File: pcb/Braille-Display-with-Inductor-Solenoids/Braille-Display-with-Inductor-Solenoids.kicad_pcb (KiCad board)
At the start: 2 copper layers, 90 x 89 mm, 203 parts, among them J1 Screw_Terminal_01x02, J2 Screw_Terminal_01x02, J3 Screw_Terminal_01x02, J4 Conn_01x03, J5 Conn_01x02, J6 Conn_01x08, SW1 SW_Push, SW2 SW_Push, U1 RP2040-Zero, U10 AD116, U11 AD116, U12 AD116, U13 AD116, U14 AD116, U15 AD116, U16 AD116, U17 AD116, U18 AD116, U19 AD116, U2 AD116, U20 AD116, U21 AD116, U22 AD116, U23 AD116, U24 AD116, U25 AD116, U26 74HC595, U27 74HC595, U28 74HC595, U29 74HC595, U3 AD116, U30 74HC595, U31 74HC595, U4 AD116, U5 AD116, U6 AD116, U7 AD116, U8 AD116, U9 AD116

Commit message: Clean up reference designator silkscreens, add layers
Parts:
- C1: moved to F.Cu
- moved U28 51.8 mm to (37.0, 76.0), turned to 180 degrees
- moved U27 50.3 mm to (37.0, 89.5), turned to 180 degrees
- moved U26 49.0 mm to (37.0, 103.5), turned to 180 degrees
- moved U29 17.4 mm to (83.0, 103.5), turned to 0 degrees
- moved U30 12.0 mm to (83.0, 89.5), turned to 0 degrees
- moved U31 7.18 mm to (83.0, 76.0), turned to 0 degrees
- moved D1 2.48 mm to (95.6, 114.5)
- moved R1 2.48 mm to (95.6, 118.4)
- moved J3 1.50 mm to (102.0, 115.5)
- moved C1 1.22 mm to (107.8, 105.2)
- moved H4 1.00 mm to (115.0, 115.0)
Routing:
- net /UART0_TX: track 0.00 -> 6.19 mm
- net /UART0_RX: track 0.00 -> 6.00 mm
- net +3V3: track 0.00 -> 1.76 mm, vias 0 -> 7
- net VDC: vias 0 -> 24
- net GND: vias 0 -> 30
- added copper zone on B.Cu, net +3V3
- added copper zone on In2.Cu, net GND
- added copper zone on In1.Cu, net VDC
- removed copper zone on B.Cu, net GND
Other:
- board size 90 x 89 mm -> 90 x 90 mm
- copper layers 2 -> 4
- board text added: "2.5mm Intra-Cell Pitch. 6mm Inter-Cell Pitch X. For 0805 (2012 Metric) vertical SMD, chip is 2mm long. Use 1.6mm PCB. Top (Red) = GND In1 (Green) = VDC In2 (Orange) = GND Bottom (Blue) = 3V3"
- board text removed: "2.5mm Intra-Cell Pitch. 6mm Inter-Cell Pitch X. For 0805 (2012 Metric) vertical SMD, chip is 2mm long. Use 1.6mm PCB."

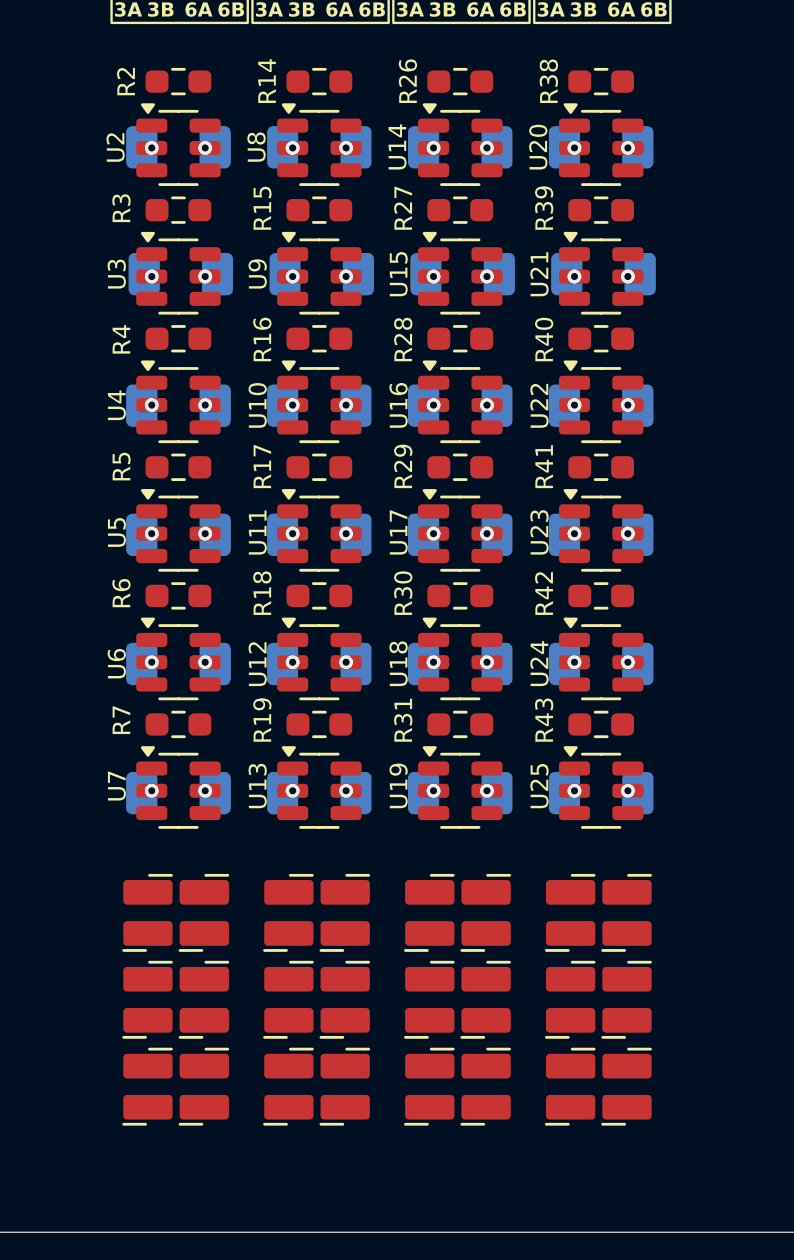
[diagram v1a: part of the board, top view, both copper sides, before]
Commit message: Fix braille LED swap
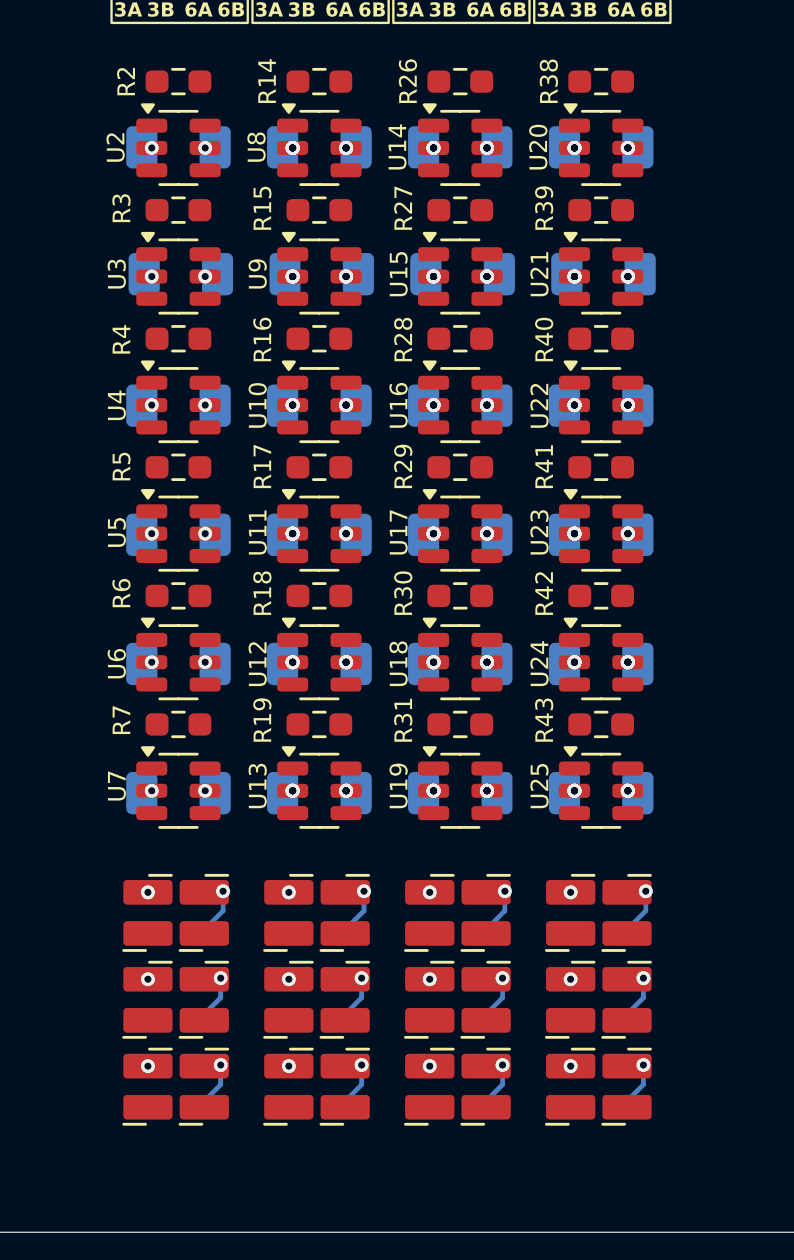
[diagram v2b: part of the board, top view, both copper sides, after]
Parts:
- moved D11 7.40 mm to (58.3, 106.4)
- moved D17 7.40 mm to (64.3, 106.4)
- moved D23 7.40 mm to (70.3, 106.4)
- moved D5 7.40 mm to (52.3, 106.4)
- moved D13 3.70 mm to (58.3, 113.8)
- moved D19 3.70 mm to (64.3, 113.8)
- moved D25 3.70 mm to (70.3, 113.8)
- moved D7 3.70 mm to (52.3, 113.8)
- moved D12 3.70 mm to (58.3, 110.1)
- moved D18 3.70 mm to (64.3, 110.1)
- moved D24 3.70 mm to (70.3, 110.1)
- moved D6 3.70 mm to (52.3, 110.1)
- turned R13 to 0 degrees
- turned R25 to 0 degrees
- turned R37 to 0 degrees
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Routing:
- net Net-(D7-AK): track 0.00 -> 2.23 mm, vias 0 -> 1
- net Net-(D6-AK): track 0.00 -> 2.23 mm, vias 0 -> 1
- net Net-(D25-AK): track 0.00 -> 2.23 mm, vias 0 -> 1
- net Net-(D24-AK): track 0.00 -> 2.23 mm, vias 0 -> 1
- net Net-(D19-AK): track 0.00 -> 2.23 mm, vias 0 -> 1
- net Net-(D18-AK): track 0.00 -> 2.23 mm, vias 0 -> 1
- net Net-(D13-AK): track 0.00 -> 2.23 mm, vias 0 -> 1
- net Net-(D12-AK): track 0.00 -> 2.23 mm, vias 0 -> 1
- net Net-(D5-AK): track 0.00 -> 2.23 mm, vias 0 -> 1
- net Net-(D11-AK): track 0.00 -> 2.23 mm, vias 0 -> 1
- net Net-(D23-AK): track 0.00 -> 2.23 mm, vias 0 -> 1
- net Net-(D17-AK): track 0.00 -> 2.23 mm, vias 0 -> 1
- net VDC: vias 24 -> 60
- net Net-(D9-AK): vias 0 -> 1
- net Net-(D8-AK): vias 0 -> 1
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
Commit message: Finish routing and review
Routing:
- net GND: track 0.00 -> 361.1 mm, vias 66 -> 41
- net VDC: track 0.00 -> 201.3 mm, vias 60 -> 29
- net +3V3: track 1.76 -> 182.3 mm, vias 7 -> 10
- net /~{SHIFT_SRCLR}: track 0.00 -> 148.0 mm, vias 0 -> 6
- net /SHIFT_RCLK: track 0.00 -> 142.7 mm, vias 0 -> 5
- net /SHIFT_SRCK: track 0.00 -> 141.2 mm, vias 0 -> 6
- net /~{SHIFT_OE}: track 0.00 -> 136.5 mm, vias 0 -> 2
- net /SHIFT_SER_IN: track 0.00 -> 92.4 mm, vias 0 -> 1
- net Net-(U28-QH'): track 0.00 -> 83.9 mm, vias 0 -> 3
- net Net-(B3-6B): track 0.00 -> 71.3 mm, vias 0 -> 2
- net /Braille_Cells_and_Controls/Braille_Cell3/DOT6_A: track 0.00 -> 70.9 mm, vias 0 -> 3
- net Net-(B4-6B): track 0.00 -> 70.8 mm, vias 0 -> 2
- net /Braille_Cells_and_Controls/Braille_Cell1/DOT6_A: track 0.00 -> 70.7 mm, vias 0 -> 3
- net /Braille_Cells_and_Controls/Braille_Cell3/DOT5_A: track 0.00 -> 70.6 mm, vias 0 -> 4
- net Net-(B4-4B): track 0.00 -> 70.2 mm, vias 0 -> 2
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- added copper zone on F.Cu, net +5V

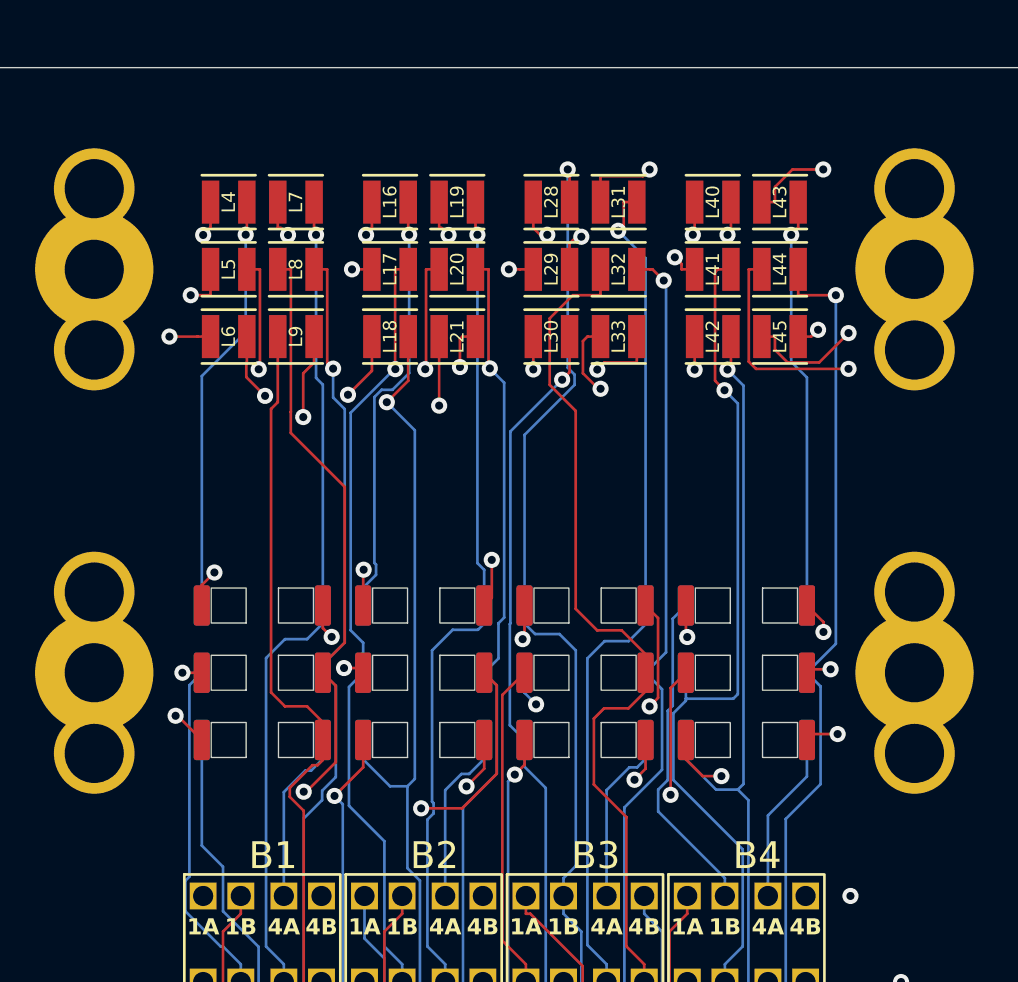
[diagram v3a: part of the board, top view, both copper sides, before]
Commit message: Update SMD solenoid with THT pads
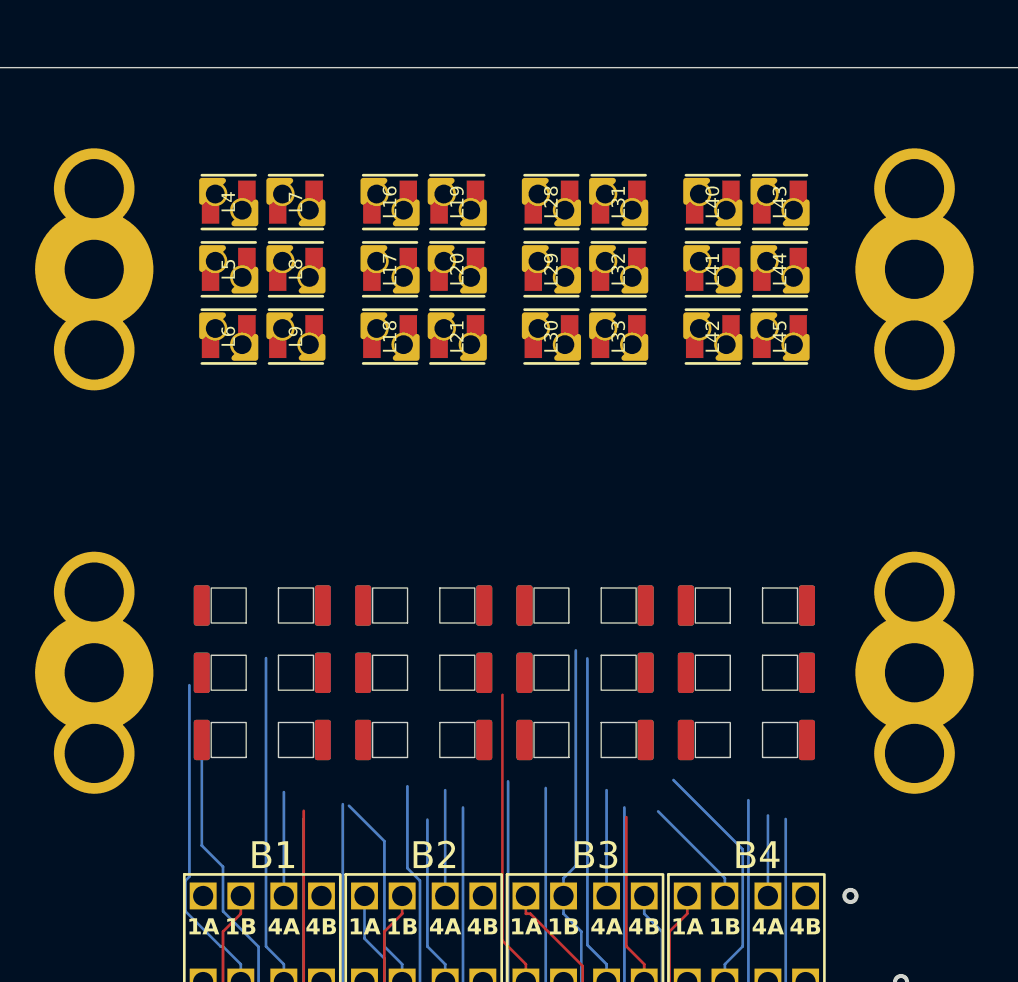
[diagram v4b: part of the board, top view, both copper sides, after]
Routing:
- net Net-(B4-4B): track 70.2 -> 27.8 mm, vias 2 -> 1
- net Net-(B2-1B): track 51.9 -> 14.2 mm, vias 1 -> 0
- net Net-(B4-1B): track 49.4 -> 16.6 mm, vias 2 -> 1
- net Net-(B1-1B): track 51.3 -> 23.3 mm, vias 1 -> 0
- net /Braille_Cells_and_Controls/Braille_Cell1/DOT5_A: track 69.2 -> 41.3 mm, vias 3 -> 1
- net /Braille_Cells_and_Controls/Braille_Cell2/DOT4_A: track 65.3 -> 38.3 mm, vias 3 -> 1
- net /Braille_Cells_and_Controls/Braille_Cell3/DOT2_A: track 50.2 -> 24.2 mm, vias 3 -> 1
- net /Braille_Cells_and_Controls/Braille_Cell2/DOT5_A: track 65.4 -> 39.8 mm
- net Net-(B2-4B): track 57.3 -> 32.7 mm, vias 2 -> 1
- net Net-(B3-6B): track 71.3 -> 47.7 mm, vias 2 -> 1
- net Net-(B4-6B): track 70.8 -> 47.4 mm, vias 2 -> 1
- net /Braille_Cells_and_Controls/Braille_Cell2/DOT1_A: track 41.9 -> 18.8 mm, vias 2 -> 0
- net Net-(B4-5B): track 59.2 -> 36.2 mm, vias 2 -> 1
- net Net-(B4-2B): track 47.5 -> 24.7 mm, vias 2 -> 1
- net Net-(B1-5B): track 60.0 -> 37.8 mm, vias 2 -> 1
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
